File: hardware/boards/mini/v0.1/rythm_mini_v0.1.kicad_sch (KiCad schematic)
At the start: 62 parts, among them IC1 NAU88C22YG, IC2 IS42S32160F-6BLI, U1 W25Q128JVP, U2 LTV-217-G, U3 RythmMini, U7 STM32H750IBKx, Y2 Crystal_GND24

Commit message: mini: route qspi flash and add more brakeout pads
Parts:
- added C34, C35: C, symbol Device:C_Small
- added R15, R16: R, Resistor_SMD:R_0402_1005Metric, symbol Device:R
- D3: JLC (none) -> C2128
- IC1: JLC (none) -> C914209
- IC2: JLC (none) -> C1348852
- U1: JLC (none) -> C190862
- U2: JLC (none) -> C17407902
- U3: now left out of the parts list
- U7: JLC (none) -> C730200
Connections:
- net +3.3V: now also R16.1
- net GND: now also D1.1 (K), D2.1 (K), U3.Y1 (GND), Y2.2, Y2.4, C34.1, C35.1
- net I2C_SCL: now also U3.C1 (PB7/SCL)
- net I2C_SDA: now also U3.B1 (PB8/SDA)
- net RST: now also U3.G1 (RESET); no longer U3.F8 (RESET)
- net VBAT: now also U3.F1 (VBAT)
- net at U7.H1 (PH1), Y2.1: now also C35.2
- net at U7.G1 (PH0), Y2.3: now also C34.2
- net LED_STATUS: now reaches U7.H15 (PC6)
- net LED_STATUS: now also R15.1
- net at D1.2 (A): now also R16.2
- net at D2.2 (A): now also R15.2
- net PA5/SCK renamed PA5
- net PA5: now also U3.M1 (PA5/SCK)
- net PA6/MISO renamed PA6
- net PA6: now also U3.N1 (PA6/MISO)
- net PA7/MOSI renamed PA7
- net PA7: now also U3.O1 (PA7/MOSI)
- net PB5/RX renamed PB5
- net PB5: now also U3.E1 (PB5/RX)
- net PB6/TX renamed PB6
- net PB6: now also U3.D1 (PB6/TX)
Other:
- note removed: "TODO: correct symbol"
- moved on the sheet: C1, C10, C11, C12, C13, C14, C2, C3, C4, C5, C6, C7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

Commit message: re-routing audio codec
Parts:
- added C36, C37: 2.2 uF <100 mΩ ESR, Capacitor_SMD:C_0402_1005Metric, symbol Device:C
- added D4: STATUS2, LED_SMD:LED_0402_1005Metric, symbol Device:LED
- added F1: Polyfuse, Fuse:Fuse_0805_2012Metric, symbol Device:Polyfuse
- added Q1: PMV37EN22, Package_TO_SOT_SMD:TSOT-23, symbol Transistor_FET:Q_NMOS_GSD
- added R17: R, Resistor_SMD:R_0402_1005Metric, symbol Device:R
- added TP1: GND, TestPoint:TestPoint_Pad_D1.0mm, symbol Connector:TestPoint
- added TP2: 3v3, TestPoint:TestPoint_Pad_D1.0mm, symbol Connector:TestPoint
- R1, R2: footprint Capacitor_SMD:C_0402_1005Metric -> Resistor_SMD:R_0402_1005Metric
- U3: footprint Library:RythmMini -> Rythm:RythmMini-v0.1; symbol Library:RythmMini -> Rythm:RythmMini-v0.1; now in the parts list
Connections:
- net +3.3V: now also F1.1; no longer U3. (3.3v)
- net GND: now also C36.2, C37.2, D4.1 (K), Q1.2 (S), TP1.1; no longer U3.A1 (GND), U3.A9 (GND), U3.Y1 (GND), U3.Y9 (GND)
- net HPL: now also U3.A6 (HPL); no longer U3.A5 (HPL)
- net HPR: now also U3.A7 (HPR); no longer U3.A6 (HPR)
- net MICL: now also U3.A4 (MICL); no longer U3.A3 (MICL)
- net MICR: now also U3.A5 (MICR); no longer U3.A4 (MICR)
- net PB13: now also U3.Q9 (PB13)
- net SPKL: now also U3.A8 (SPKL); no longer U3.A7 (SPKL)
- net SPKR: now also U3.A9 (NC); no longer U3.A8 (SPKR)
- net LED_STATUS2: now reaches U7.D15 (PA10)
- net LED_STATUS2: now also R17.1
- net at U7.F13 (VCAP): now also C37.1
- net at U7.M10 (VCAP): now also C36.1
- net LIN: now reaches IC1.3 (LLIN/GPIO2)
- net LIN: now also U3.A2 (IN_L)
- net RIN: now reaches IC1.6 (RLIN/GPIO3)
- net RIN: now also U3.A3 (IN_R)
- new net: D4.2 (A), R17.2
- new net: U3.A1 (NC), U3.A9 (NC), U3.Y1 (NC), U3.Y9 (NC)
- new net 3v3+: F1.2, Q1.1 (G), TP2.1, U3.T9 (3.3v)
- new net 3v3_GND: Q1.3 (D), U3.R9 (GND)
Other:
- note added: "Reverse voltage protection circuit"
- note removed: "VBUS SDMMC SAI"

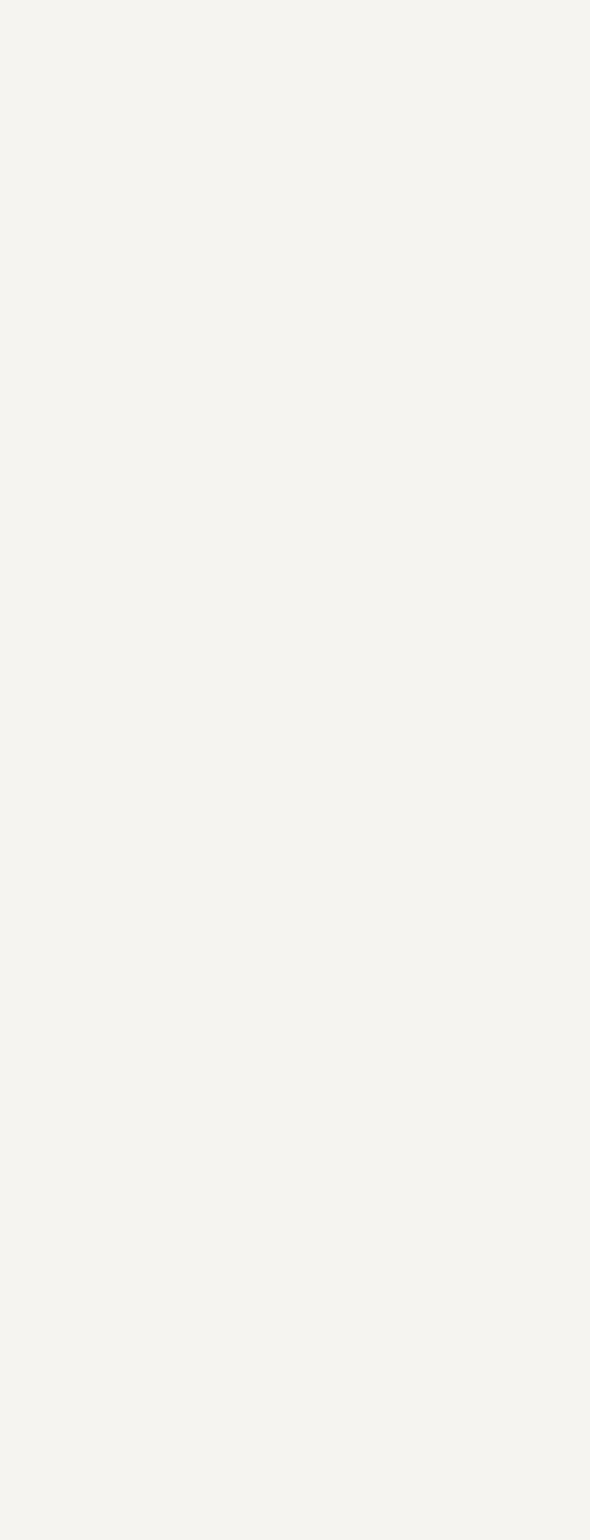
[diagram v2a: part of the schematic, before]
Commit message: start adding README.md
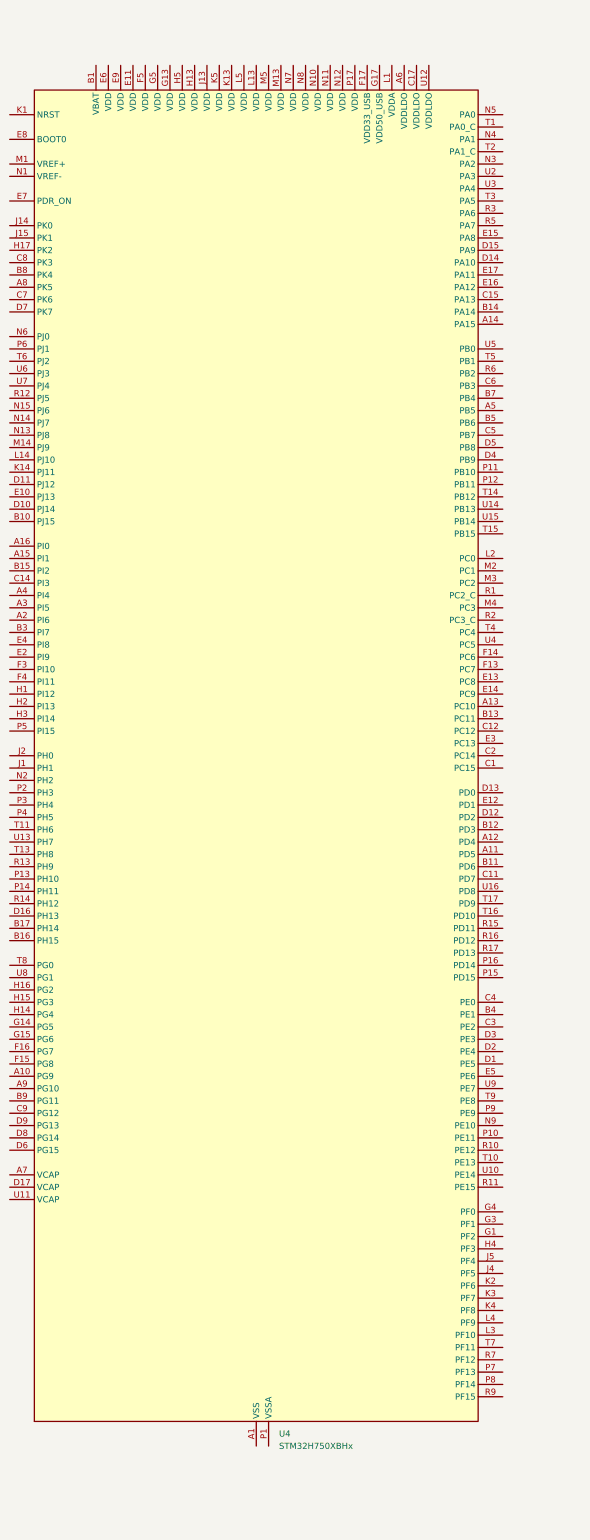
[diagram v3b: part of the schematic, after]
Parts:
- added U4: STM32H750XBHx, Package_BGA:TFBGA-265_14x14mm_Layout17x17_P0.8mm, symbol MCU_ST_STM32H7:STM32H750XBHx
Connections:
- new net: U4.A1 (VSS), U4.A17 (VSS), U4.B2 (VSS), U4.B6 (VSS), U4.C10 (VSS), U4.C13 (VSS), U4.C16 (VSS), U4.F1 (VSS), U4.F2 (VSS), U4.G10 (VSS), U4.G11 (VSS), U4.G16 (VSS), U4.G2 (VSS), U4.G7 (VSS), U4.G8 (VSS), U4.G9 (VSS), U4.H10 (VSS), U4.H11 (VSS), U4.H7 (VSS), U4.H8 (VSS), U4.H9 (VSS), U4.J10 (VSS), U4.J11 (VSS), U4.J16 (VSS), U4.J17 (VSS), U4.J3 (VSS), U4.J7 (VSS), U4.J8 (VSS), U4.J9 (VSS), U4.K10 (VSS), U4.K11 (VSS), U4.K15 (VSS), U4.K7 (VSS), U4.K8 (VSS), U4.K9 (VSS), U4.L10 (VSS), U4.L11 (VSS), U4.L15 (VSS), U4.L7 (VSS), U4.L8 (VSS), U4.L9 (VSS), U4.M15 (VSS), U4.N16 (VSS), U4.R4 (VSS), U4.R8 (VSS), U4.T12 (VSS), U4.U1 (VSS), U4.U17 (VSS)
